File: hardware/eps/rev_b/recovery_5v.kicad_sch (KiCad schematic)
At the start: 34 parts, among them U500 TPS 552872

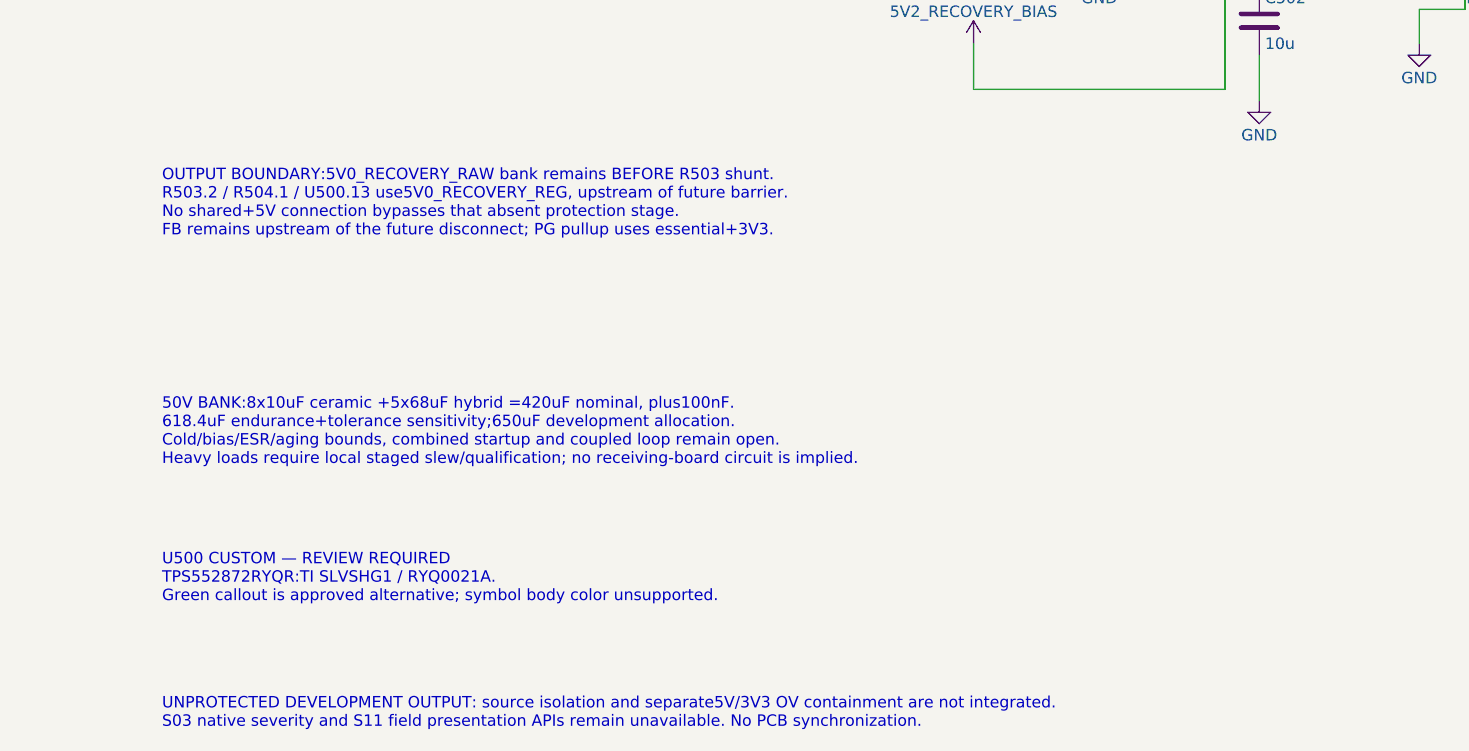
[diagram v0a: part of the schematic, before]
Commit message: Integrate solar and recovery rail protection into EPS Rev B
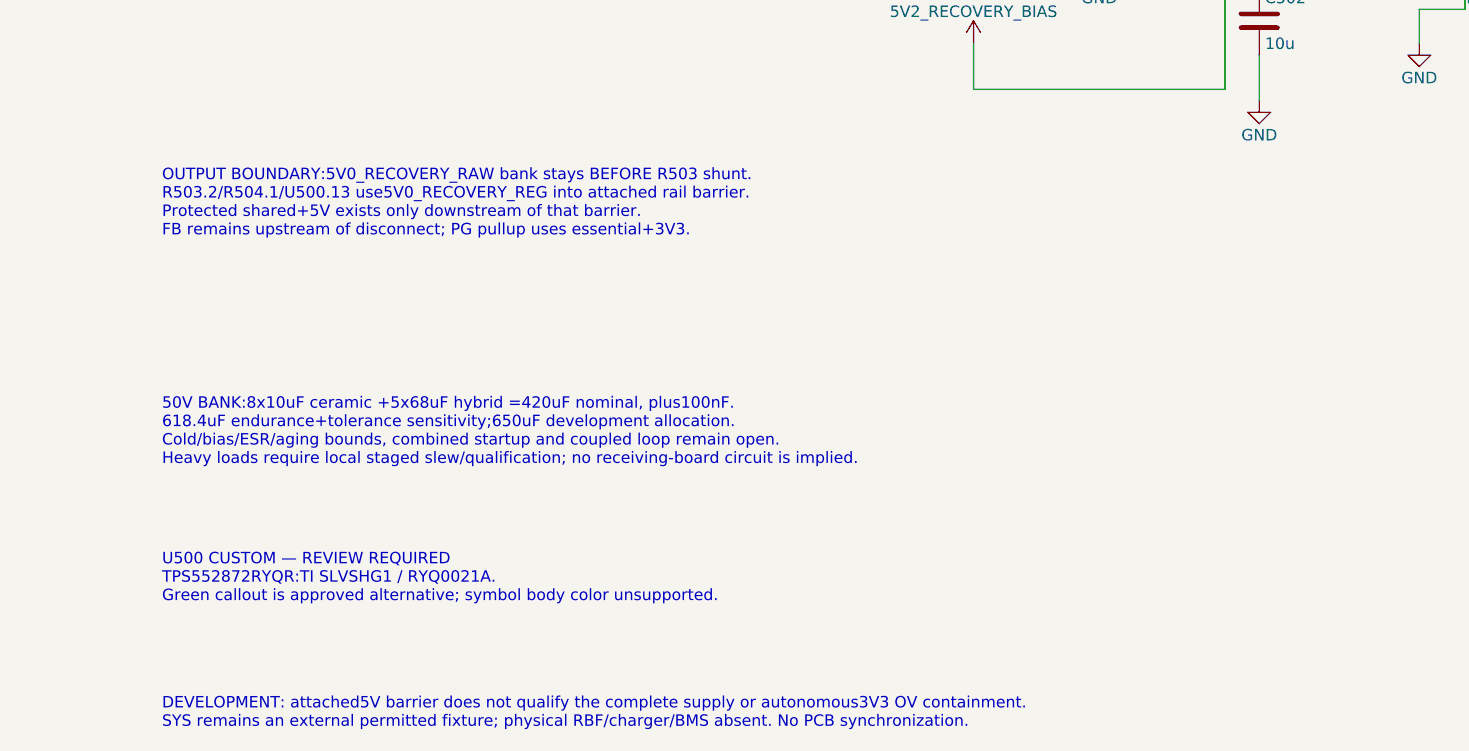
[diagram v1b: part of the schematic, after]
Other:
- note added: "DEVELOPMENT: attached5V barrier does not qualify the complete supply or autonomous3V3 OV containment. SYS remains an external permitted fixture; physical RBF/charger/BMS absent. No PCB synchronization."
- note added: "OUTPUT BOUNDARY:5V0_RECOVERY_RAW bank stays BEFORE R503 shunt. R503.2/R504.1/U500.13 use5V0_RECOVERY_REG into attached rail barrier. Protected shared+5V exists only downstream of that barrier. FB remains upstream of disconnect; PG pullup uses essential+3V3."
- note removed: "OUTPUT BOUNDARY:5V0_RECOVERY_RAW bank remains BEFORE R503 shunt. R503.2 / R504.1 / U500.13 use5V0_RECOVERY_REG, upstream of future barrier. No shared+5V connection bypasses that absent protection stage. FB remains upstream of the future disconnect; PG pullup uses essential+3V3."
- note removed: "UNPROTECTED DEVELOPMENT OUTPUT: source isolation and separate5V/3V3 OV containment are not integrated. S03 native severity and S11 field presentation APIs remain unavailable. No PCB synchronization."
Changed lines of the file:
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@@
-    (effects (font (size 1.27 1.27)) (justify left bottom))
-  )
-  (text "OUTPUT BOUNDARY:5V0_RECOVERY_RAW bank remains BEFORE R503 shunt.\nR503.2 / R504.1 / U500.13 use5V0_RECOVERY_REG, upstream of future barrier.\nNo shared+5V connection bypasses that absent protection stage.\nFB remains upstream of the future disconnect; PG pullup uses essential+3V3."
-    (at 40.64 184.15 0)
     (effects (font (size 1.27 1.27)) (justify left bottom))
   )
@@
     (effects (font (size 1.27 1.27)) (justify left bottom))
   )
-  (text "UNPROTECTED DEVELOPMENT OUTPUT: source isolation and separate5V/3V3 OV containment are not integrated.\nS03 native severity and S11 field presentation APIs remain unavailable. No PCB synchronization."
-    (at 40.64 238.76 0)
-    (effects (font (size 1.27 1.27)) (justify left bottom))
-  )
   (text "U500 CUSTOM — REVIEW REQUIRED\nTPS552872RYQR:TI SLVSHG1 / RYQ0021A.\nGreen callout is approved alternative; symbol body color unsupported."
     (at 40.64 224.79 0)
     (effects (font (size 1.27 1.27) (color 0 255 0 1)) (justify left bottom))
   )
+  (text "OUTPUT BOUNDARY:5V0_RECOVERY_RAW bank stays BEFORE R503 shunt.\nR503.2/R504.1/U500.13 use5V0_RECOVERY_REG into attached rail barrier.\nProtected shared+5V exists only downstream of that barrier.\nFB remains upstream of disconnect; PG pullup uses essential+3V3."
+    (at 40.64 184.15 0)
+    (effects (font (size 1.27 1.27)) (justify left bottom))
+  )
+  (text "DEVELOPMENT: attached5V barrier does not qualify the complete supply or autonomous3V3 OV containment.\nSYS remains an external permitted fixture; physical RBF/charger/BMS absent. No PCB synchronization."
+    (at 40.64 238.76 0)
+    (effects (font (size 1.27 1.27)) (justify left bottom))
+  )
 	(symbol

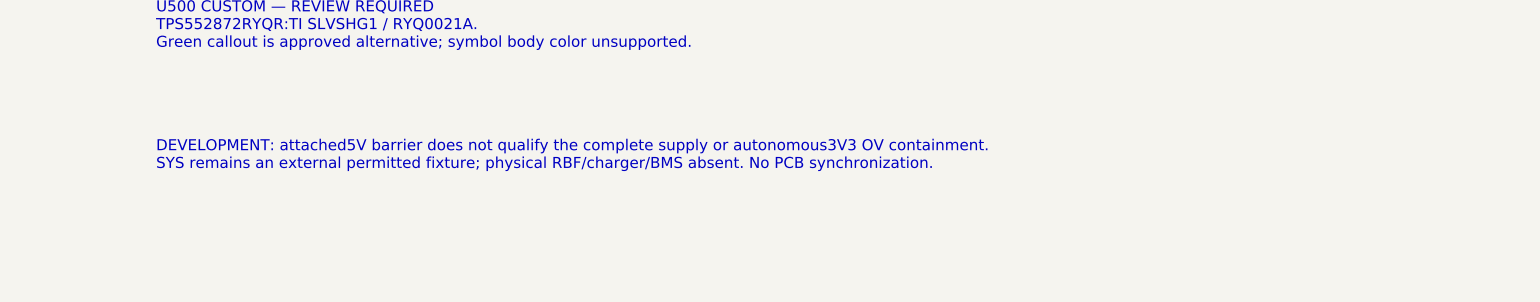
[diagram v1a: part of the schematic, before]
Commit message: Integrate LTC4162 charger PowerPath and thermistor interface into EPS Rev B
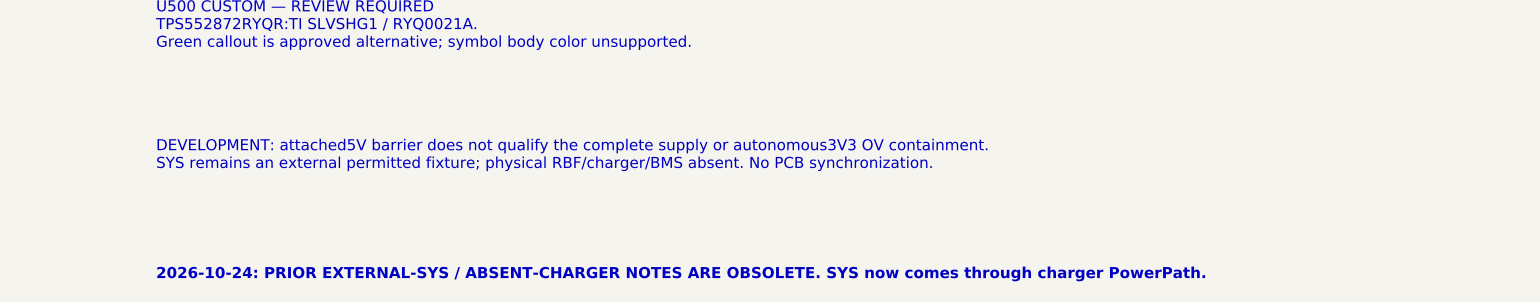
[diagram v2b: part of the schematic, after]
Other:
- note added: "2026-10-24: PRIOR EXTERNAL-SYS / ABSENT-CHARGER NOTES ARE OBSOLETE. SYS now comes through charger PowerPath."
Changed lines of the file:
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@@
     (effects (font (size 1.27 1.27)) (justify left bottom))
+  )
+  (text "2026-10-24: PRIOR EXTERNAL-SYS / ABSENT-CHARGER NOTES ARE OBSOLETE. SYS now comes through charger PowerPath."
+    (at 40.64 251.46 0)
+    (effects (font (size 1.27 1.27) (bold yes)) (justify left bottom))
   )
 	(symbol

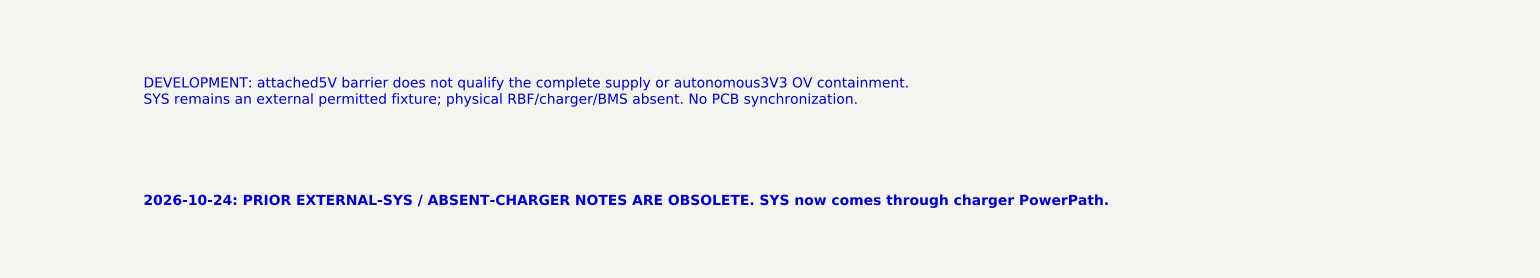
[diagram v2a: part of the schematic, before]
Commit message: Integrate EPS Rev B battery management development circuit
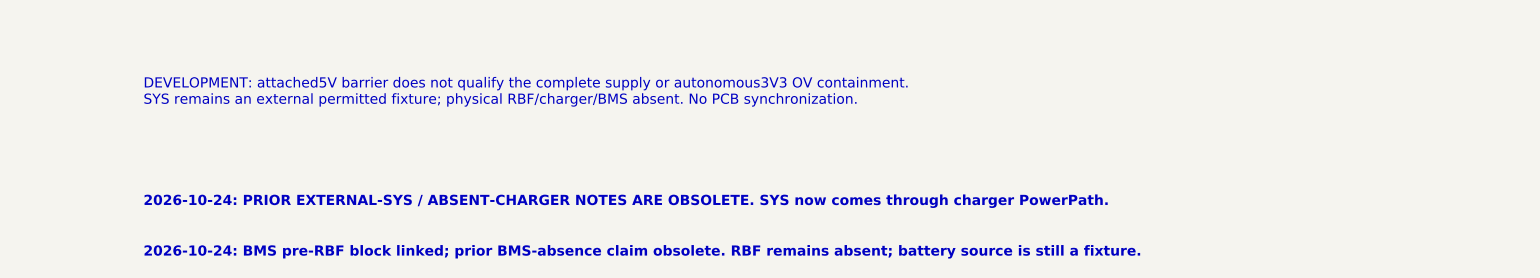
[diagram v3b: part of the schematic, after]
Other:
- note added: "2026-10-24: BMS pre-RBF block linked; prior BMS-absence claim obsolete. RBF remains absent; battery source is still a fixture."
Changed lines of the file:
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@@
+    (effects (font (size 1.27 1.27) (bold yes)) (justify left bottom))
+  )
+  (text "2026-10-24: BMS pre-RBF block linked; prior BMS-absence claim obsolete. RBF remains absent; battery source is still a fixture."
+    (at 40.64 257.81 0)
     (effects (font (size 1.27 1.27) (bold yes)) (justify left bottom))
   )
